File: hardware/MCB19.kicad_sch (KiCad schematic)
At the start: 1 part

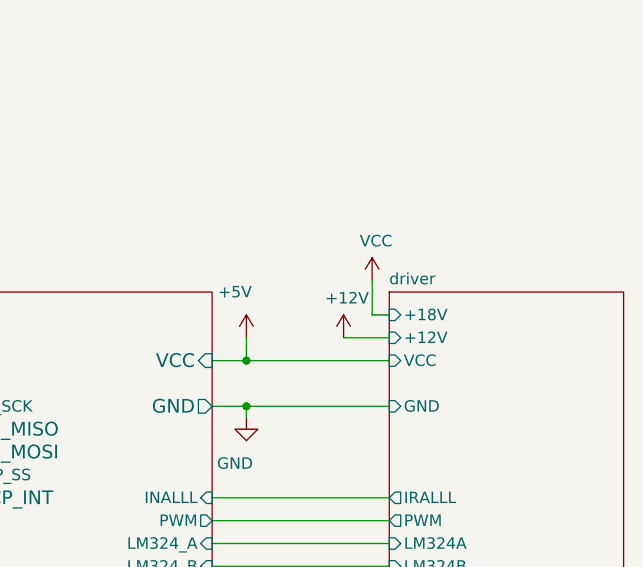
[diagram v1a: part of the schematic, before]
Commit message: add diode protections for Vsense OpAmps and uC port
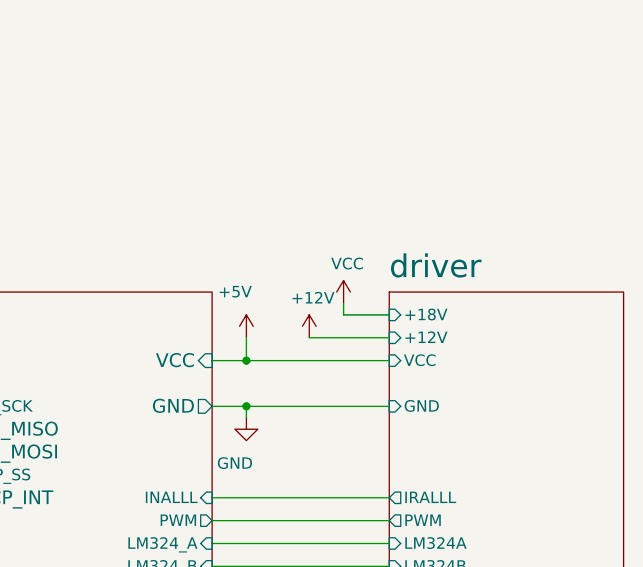
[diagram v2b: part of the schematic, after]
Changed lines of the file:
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@@
 	(wire
 		(pts
-			(xy 198.755 92.71) (xy 198.755 96.52)
+			(xy 195.58 95.25) (xy 195.58 96.52)
 		)
 		(stroke
@@
 	(wire
 		(pts
-			(xy 198.755 96.52) (xy 200.66 96.52)
+			(xy 195.58 96.52) (xy 200.66 96.52)
 		)
 		(stroke
@@
 	(wire
 		(pts
-			(xy 195.58 99.06) (xy 200.66 99.06)
+			(xy 191.77 99.06) (xy 200.66 99.06)
 		)
 		(stroke
@@
 	(symbol
 		(lib_id "power:+12V")
-		(at 195.58 99.06 0)
+		(at 191.77 99.06 0)
 		(unit 1)
 		(exclude_from_sim no)
@@
 		(dnp no)
 		(property "Reference" "#PWR0112"
-			(at 195.58 102.87 0)
+			(at 191.77 102.87 0)
 			(effects
 				(font
@@
 		)
 		(property "Value" "+12V"
-			(at 195.961 94.6658 0)
+			(at 192.151 94.6658 0)
 			(effects
 				(font
@@
 		)
 		(property "Footprint" ""
-			(at 195.58 99.06 0)
+			(at 191.77 99.06 0)
 			(effects
 				(font
@@
 		)
 		(property "Datasheet" ""
-			(at 195.58 99.06 0)
+			(at 191.77 99.06 0)
 			(effects
 				(font
@@
 		)
 		(property "Description" ""
-			(at 195.58 99.06 0)
+			(at 191.77 99.06 0)
 			(effects
 				(font
@@
 	(symbol
 		(lib_id "power:VCC")
-		(at 198.755 92.71 0)
+		(at 195.58 95.25 0)
 		(unit 1)
 		(exclude_from_sim no)
@@
 		(dnp no)
 		(property "Reference" "#PWR0120"
-			(at 198.755 96.52 0)
+			(at 195.58 99.06 0)
 			(effects
 				(font
@@
 		)
 		(property "Value" "VCC"
-			(at 199.1868 88.3158 0)
+			(at 196.0118 90.8558 0)
 			(effects
 				(font
@@
 		)
 		(property "Footprint" ""
-			(at 198.755 92.71 0)
+			(at 195.58 95.25 0)
 			(effects
 				(font
@@
 		)
 		(property "Datasheet" ""
-			(at 198.755 92.71 0)
+			(at 195.58 95.25 0)
 			(effects
 				(font
@@
 		)
 		(property "Description" ""
-			(at 198.755 92.71 0)
+			(at 195.58 95.25 0)
 			(effects
 				(font
@@
 		)
 		(property "Sheetname" "driver"
-			(at 200.66 93.2684 0)
-			(effects
-				(font
-					(size 1.27 1.27)
+			(at 200.66 92.6334 0)
+			(effects
+				(font
+					(size 2.54 2.54)
 				)
 				(justify left bottom)
